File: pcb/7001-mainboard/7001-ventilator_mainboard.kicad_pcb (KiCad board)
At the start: 4 copper layers, 20 x 159.7 mm, 148 parts, among them J1 USB_B_Micro, J2 DNI (2211R-03G-SM-CR ), J3 Conn_01x02_MountingPin, J4 Conn_01x02_MountingPin, J5 Conn_01x02_MountingPin, Q1 IRLML6244TRPbF, Q10 SiA469DJ, Q2 IRLML6244TRPbF, Q3 IRLML6244TRPbF, Q4 2N7002P,215, Q5 2N7002P,215, Q6 DMP2035U, Q7 DMP2035U, Q8 2N7002P,215, Q9 2N7002P,215, SW1 SKQYABE010, U1 LPC11U37FBD48-401_, U10 MIC5501-3.0YM5, U11 NCP551SN50T1G, U12 74AHCT1G125SE, U2 MPXH6250AC6T1, U3 AT25SF041-SSHD-T, U5 TPS61087DSC, U6 BQ2002T, U7 TLV9001SIDBVR, U8 74AHCT1G125SE, U9 TPD2E2U06, Y1 MCSJK-7U-12.00-10-10-80-B-10

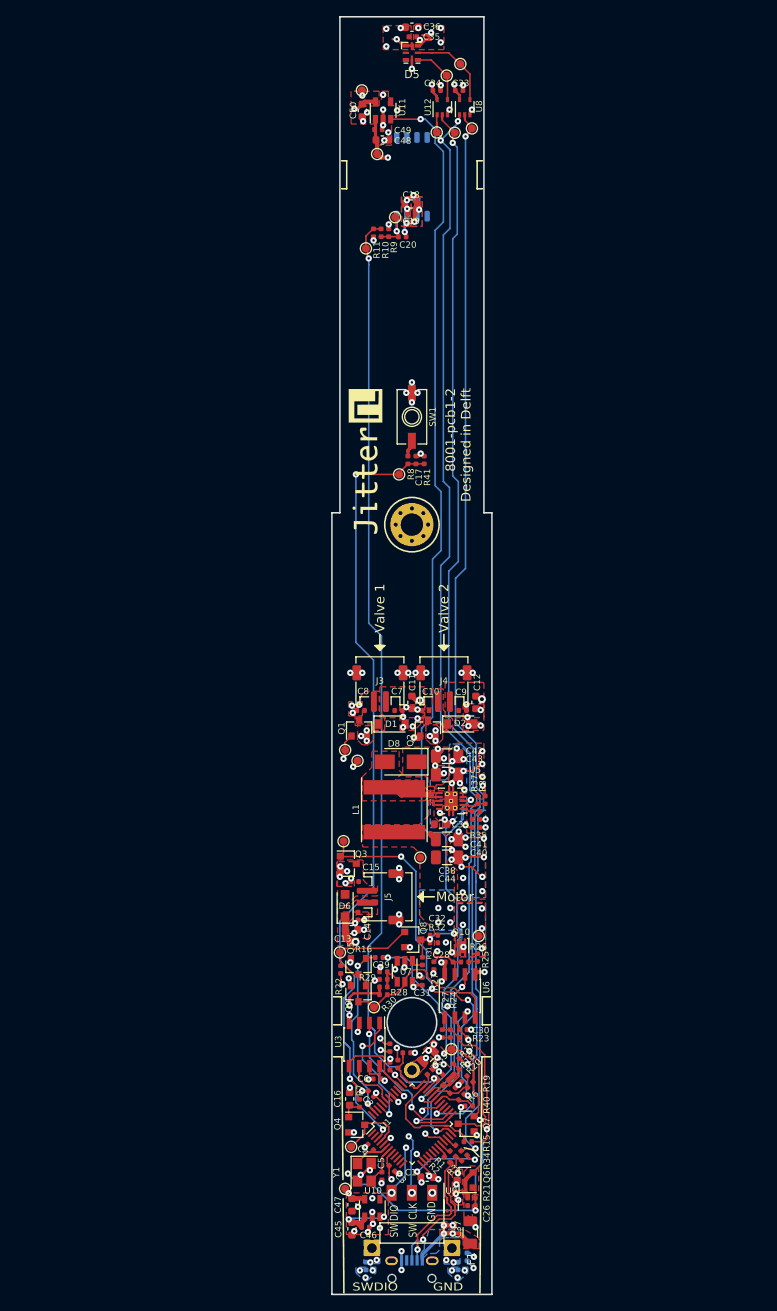
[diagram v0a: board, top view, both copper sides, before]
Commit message: Add 0-20mA for pressure regulator
The pressure regulator can be adjusted via 4-20mA (SPI via AD5410)
The regulator has an on-board pressure sensor giving 4-20mA feedback, which
we convert to 0.6-3.0V for the ADC.
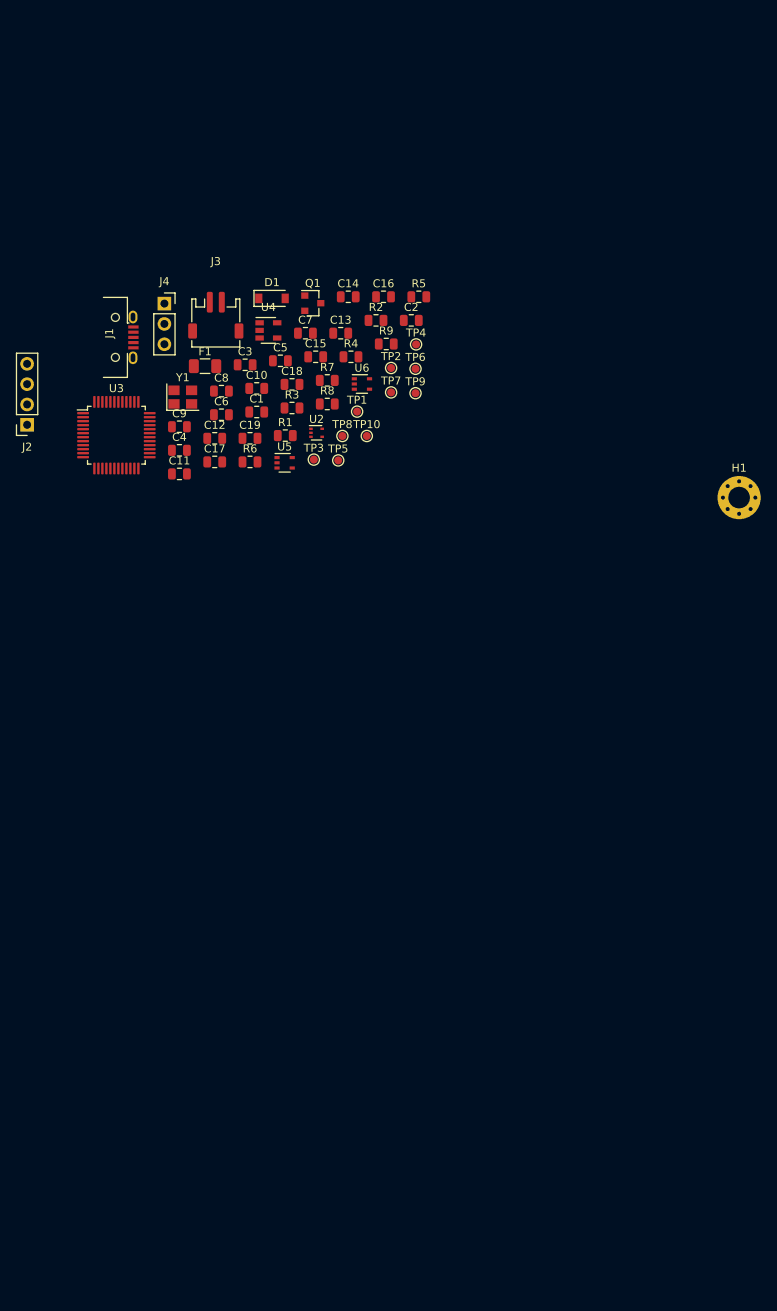
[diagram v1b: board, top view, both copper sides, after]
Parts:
- removed BT1: Battery, Jitter_Footprints:battery_varta_3V600HR
- removed C20: 47pF, Capacitor_SMD:C_0402_1005Metric
- removed C22, C24, C25, C27, C28, C29, C30, C31, C33, C34, C35, C37, C40, C46, C49: 100nF, Capacitor_SMD:C_0402_1005Metric
- removed C23, C26, C41, C51, C52: 2.2nF, Capacitor_SMD:C_0402_1005Metric
- removed C32: DNI, Capacitor_SMD:C_0402_1005Metric
- removed C36, C39, C45, C47, C48, C50: 1uF, Capacitor_SMD:C_0603_1608Metric
- removed C38, C42, C43, C44: 10uF eff, Capacitor_SMD:C_1206_3216Metric
- removed D2: BZT52C10+, Diode_SMD:D_SOD-123
- removed D5: APA102-2020, Jitter_Footprints:LED_APA102-2020
- removed D6: NRVTS245ESFT3G, Diode_SMD:D_SOD-123F
- removed D8: B340A-13-F, Diode_SMD:D_SMA
- removed G***: LOGO, Jitter_Logos:Jitter-med
- removed J5: Conn_01x02_MountingPin, Jitter_Footprints:JST_ZH_S2B-ZR-SM4A-TF_1x02-1MP_P1.5mm_Horizontal
- removed L1: 4.7uH, Jitter_Footprints:Inductor_Taiyo-Yuden_NR-8030
- removed Q10: SiA469DJ, Jitter_Footprints:Vishay_PowerPAK_SC70-6L_Single
- removed Q2, Q3: IRLML6244TRPbF, Package_TO_SOT_SMD:SOT-23
- removed Q4, Q5, Q8, Q9: 2N7002P,215, Package_TO_SOT_SMD:SOT-23
- removed Q6, Q7: DMP2035U, Package_TO_SOT_SMD:SOT-23
- removed R10, R36: 68k, Resistor_SMD:R_0402_1005Metric
- removed R11, R21, R32: 100k, Resistor_SMD:R_0402_1005Metric
- removed R15, R16, R18, R20, R25, R26, R27, R28, R30, R41: 1M, Resistor_SMD:R_0402_1005Metric
- removed R17, R19: 680k, Resistor_SMD:R_0402_1005Metric
- removed R22, R23, R24: 12k, Resistor_SMD:R_0402_1005Metric
- removed R29: 11k, Resistor_SMD:R_0402_1005Metric
- removed R31, R34: 100, Resistor_SMD:R_0402_1005Metric
- removed R33: 0.056, Resistor_SMD:R_0805_2012Metric
- removed R35: 8.2k, Resistor_SMD:R_0402_1005Metric
- removed R37: 17.4k, Resistor_SMD:R_0402_1005Metric
- removed R38, R39, R40: 4.7k, Resistor_SMD:R_0402_1005Metric
- removed SW1: SKQYABE010, Jitter_Footprints:SW_SPST_SKQYABE010
- removed TH1: B57230V2103F260 (10K), Resistor_SMD:R_0402_1005Metric
- removed TP11: valve_1_fet, TestPoint:TestPoint_Pad_D1.0mm
- removed TP12: valve_2_fet, TestPoint:TestPoint_Pad_D1.0mm
- removed TP13: motor_fet, TestPoint:TestPoint_Pad_D1.0mm
- removed TP14: sensor_out, TestPoint:TestPoint_Pad_D1.0mm
- removed TP15: pressure_level, TestPoint:TestPoint_Pad_D1.0mm
- removed TP16: LED_~CS~, TestPoint:TestPoint_Pad_D1.0mm
- removed TP17: LED_CLK, TestPoint:TestPoint_Pad_D1.0mm
- removed TP18: LED_MOSI, TestPoint:TestPoint_Pad_D1.0mm
- removed TP19: LED_clk_5V, TestPoint:TestPoint_Pad_D1.0mm
- removed TP20: LED_data_5V, TestPoint:TestPoint_Pad_D1.0mm
- removed U1: LPC11U37FBD48-401_, Package_QFP:LQFP-48_7x7mm_P0.5mm
- removed U10: MIC5501-3.0YM5, Package_TO_SOT_SMD:SOT-23-5
- removed U11: NCP551SN50T1G, Package_TO_SOT_SMD:SOT-23-5
- removed U12, U8: 74AHCT1G125SE, Package_TO_SOT_SMD:SOT-353_SC-70-5
- removed U7: TLV9001SIDBVR, Jitter_Footprints:TSOT-23-6
- removed U9: TPD2E2U06, Package_TO_SOT_SMD:SOT-553
- added U4: MIC5501-3.0YM5, Package_TO_SOT_SMD:SOT-23-5, F.Cu at (92.1, 59.2)
- C1, C11, C16: value 1uF -> 100nF; footprint Capacitor_SMD:C_0603_1608Metric -> Capacitor_SMD:C_0805_2012Metric
- C10: value 2.2nF -> 18pF; footprint Capacitor_SMD:C_0402_1005Metric -> Capacitor_SMD:C_0805_2012Metric
- C12: value 1uF -> 18pF; footprint Capacitor_SMD:C_0603_1608Metric -> Capacitor_SMD:C_0805_2012Metric
- C13, C18: footprint Capacitor_SMD:C_0603_1608Metric -> Capacitor_SMD:C_0805_2012Metric
- C14: value 2.2nF -> 100nF; footprint Capacitor_SMD:C_0402_1005Metric -> Capacitor_SMD:C_0805_2012Metric
- C15: value 2.2nF -> 1uF; footprint Capacitor_SMD:C_0402_1005Metric -> Capacitor_SMD:C_0805_2012Metric
- C17, C2, C3, C6, C7, C9: footprint Capacitor_SMD:C_0402_1005Metric -> Capacitor_SMD:C_0805_2012Metric
- C19: value 100nF -> 2.2nF; footprint Capacitor_SMD:C_0402_1005Metric -> Capacitor_SMD:C_0805_2012Metric
- C4, C5: value 18pF -> 1uF; footprint Capacitor_SMD:C_0402_1005Metric -> Capacitor_SMD:C_0805_2012Metric
- C8: value 2.2nF -> 47pF; footprint Capacitor_SMD:C_0402_1005Metric -> Capacitor_SMD:C_0805_2012Metric
- J1: moved to F.Cu
- J2: value DNI (2211R-03G-SM-CR ) -> SWD; footprint Jitter_Footprints:header_3x2.54_right_angle -> Connector_PinSocket_2.54mm:PinSocket_1x04_P2.54mm_Vertical
- J4: value Conn_01x02_MountingPin -> DNI; footprint Jitter_Footprints:JST_ZH_S2B-ZR-SM4A-TF_1x02-1MP_P1.5mm_Horizontal -> Connector_PinSocket_2.54mm:PinSocket_1x03_P2.54mm_Vertical
- R1: value 33R -> 68k; footprint Resistor_SMD:R_0402_1005Metric -> Resistor_SMD:R_0805_2012Metric
- R2: value 33R -> 100k; footprint Resistor_SMD:R_0402_1005Metric -> Resistor_SMD:R_0805_2012Metric
- R3, R6: footprint Resistor_SMD:R_0402_1005Metric -> Resistor_SMD:R_0805_2012Metric
- R4, R5: value 1k -> 33R; footprint Resistor_SMD:R_0402_1005Metric -> Resistor_SMD:R_0805_2012Metric
- R7: value 1M -> 4.7k; footprint Resistor_SMD:R_0402_1005Metric -> Resistor_SMD:R_0805_2012Metric
- R8: value 1k -> 1k5; footprint Resistor_SMD:R_0402_1005Metric -> Resistor_SMD:R_0805_2012Metric
- R9: value DNI (51k?) -> 1k5; footprint Resistor_SMD:R_0402_1005Metric -> Resistor_SMD:R_0805_2012Metric
- TP1: value ~ISP~ -> Reset
- TP10: value 5V -> valve_2_fet
- TP2: value Reset -> sensor_out
- TP3: value Vbus -> pressure_level
- TP4: value USB_~pwr_en~ -> LED_~CS~
- TP5: value unregulated_pwr -> 3V
- TP6: value charge_constant_current -> LED_CLK
- TP7: value V_battery -> LED_clk_5V
- TP8: value 3V -> LED_MOSI
- TP9: value 6V -> LED_data_5V
- U2: value MPXH6250AC6T1 -> TPD2E2U06; footprint Jitter_Footprints:MPXH6250AC -> Package_TO_SOT_SMD:SOT-553; moved to F.Cu
- U3: value AT25SF041-SSHD-T -> LPC11U37FBD48-401_; footprint Package_SO:SOIC-8_3.9x4.9mm_P1.27mm -> Package_QFP:LQFP-48_7x7mm_P0.5mm
- U5: value TPS61087DSC -> 74AHCT1G125SE; footprint Package_SON:VSON-10-1EP_3x3mm_P0.5mm_EP1.65x2.4mm_ThermalVias -> Package_TO_SOT_SMD:SOT-353_SC-70-5
- U6: value BQ2002T -> 74AHCT1G125SE; footprint Package_SO:SOIC-8_3.9x4.9mm_P1.27mm -> Package_TO_SOT_SMD:SOT-353_SC-70-5
- moved J1 125.8 mm to (70.9, 60.1), turned to 0 degrees
- moved F1 113.2 mm to (84.1, 63.7), turned to 0 degrees
- moved J2 107.4 mm to (61.9, 71.0)
- moved R2 105.3 mm to (105.5, 58.0), turned to 0 degrees
- moved C5 102.7 mm to (93.6, 63.0), turned to 0 degrees
- moved C3 102.1 mm to (89.2, 63.5), turned to 0 degrees
- moved C16 100.4 mm to (106.5, 55.0), turned to 0 degrees
- moved Y1 99.5 mm to (81.4, 67.5), turned to 0 degrees
- moved C1 98.0 mm to (90.6, 69.4)
- moved C2 96.8 mm to (109.9, 58.0), turned to 0 degrees
- moved R3 96.2 mm to (95.0, 68.9), turned to 0 degrees
- moved R5 95.9 mm to (110.9, 55.0), turned to 0 degrees
- moved TP8 94.1 mm to (101.3, 72.4)
- moved R1 92.2 mm to (94.2, 72.3), turned to 0 degrees
- moved TP1 91.9 mm to (103.2, 69.3)
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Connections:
- C1 pad 1: +3V -> Net-(C1-Pad1)
- C10 pad 1: Net-(C10-Pad1) -> /XTAL_IN
- C11 pad 1: +6V -> +5V
- C12 pad 1: +6V -> /XTAL_OUT
- C13 pad 1: +6V -> +5V
- C14 pad 1: +6V -> +5V
- C15 pad 1: Net-(C15-Pad1) -> +3V3
- C16 pad 1: GND -> +5V
- C16 pad 2: Net-(C16-Pad2) -> GND
- C17 pad 1: /MCU/button -> +6V
- C18 pad 1: +5V -> +6V
- C19 pad 1: +5V -> Net-(C19-Pad1)
- C2 pad 1: +3V -> +3V3
- C3 pad 1: +3V -> +3V3
- C4 pad 1: /MCU/XTAL_IN -> +3V3
- C5 pad 1: /MCU/XTAL_OUT -> +5V
- C6 pad 1: +3V -> +5V
- C7 pad 1: +6V -> /~RESET~
- C8 pad 1: Net-(C8-Pad1) -> /pressure_sensor_out
- C9 pad 1: +6V -> /pressure_level
- D1 pad 1: Net-(C8-Pad1) -> Net-(C19-Pad1)
- F1 pad 1: Net-(C37-Pad1) -> Net-(C1-Pad1)
- F1 pad 2: /Battery & Power Select/Vbus -> +5V
- J1 pad 1: Net-(C37-Pad1) -> Net-(C1-Pad1)
- J1 pad 2: /MCU/USB_DN -> /USB_DN
- J1 pad 3: /MCU/USB_DP -> /USB_DP
- J1 pad 4: Net-(J1-Pad4) -> (no net)
- J2 pad 2: /MCU/SWCLK -> /SWCLK
- J2 pad 3: /MCU/SWDIO -> /SWDIO
- J3 pad 2: Net-(C8-Pad1) -> Net-(C19-Pad1)
- J4 pad 1: +6V -> GND
- J4 pad 2: Net-(C10-Pad1) -> /~ISP~
- Q1 pad 3: Net-(C8-Pad1) -> Net-(C19-Pad1)
- R1 pad 1: /MCU/USB_DP -> /pressure_level
- R1 pad 2: Net-(R1-Pad2) -> /pressure_sensor_out
- R2 pad 1: /MCU/USB_DN -> GND
- R2 pad 2: Net-(R2-Pad2) -> /pressure_level
- R3 pad 1: /MCU/USB_DP -> /USB_DP
- R3 pad 2: +3V -> +3V3
- R4 pad 1: Net-(Q1-Pad1) -> /USB_DP
- R4 pad 2: /MCU/valve_1 -> Net-(R4-Pad2)
- R5 pad 1: Net-(Q2-Pad1) -> /USB_DN
- R5 pad 2: /MCU/valve_2 -> Net-(R5-Pad2)
- R6 pad 1: Net-(Q3-Pad1) -> Net-(Q1-Pad1)
- R6 pad 2: /MCU/motor -> /pwm_1
- R7 pad 1: Net-(C16-Pad2) -> GND
- R7 pad 2: /MCU/button -> /pwm_1
- R8 pad 1: /MCU/button -> /I2C_SCL
- R8 pad 2: Net-(R8-Pad2) -> +5V
- R9 pad 1: GND -> /I2C_SDA
- R9 pad 2: /sensor/pressure_sensor_out -> +5V
- TP1 pad 1: /MCU/button_~ISP~ -> /~RESET~
- TP10 pad 1: +5V -> Net-(Q1-Pad1)
- TP2 pad 1: /MCU/button -> /pressure_sensor_out
- TP3 pad 1: /Battery & Power Select/Vbus -> /pressure_level
- TP4 pad 1: /Battery & Power Select/USB_~pwr_en~ -> /LED_~CS~
- TP5 pad 1: /Battery & Power Select/unregulated_pwr -> +3V3
- TP6 pad 1: /Battery & Power Select/charge_constant_current -> /LED_CLK
- TP7 pad 1: /Battery & Power Select/V_battery -> /LED_clock_5V
- TP8 pad 1: +3V -> /LED_MOSI
- TP9 pad 1: +6V -> /LED_data_5V
- U2 pad 1: Net-(U2-Pad1) -> (no net)
- U2 pad 2: +5V -> /USB_DN
- U2 pad 3: GND -> /USB_DP
- U2 pad 4: /sensor/pressure_sensor_out -> GND
- U2 pad 5: Net-(U2-Pad5) -> /USB_DN
- U3 pad 1: /MCU/flash_~CS~ -> (no net)
- U3 pad 2: /MCU/flash_MISO -> (no net)
- U3 pad 3: +3V -> /~RESET~
- U3 pad 4: GND -> /~ISP~
- U3 pad 5: /MCU/flash_MOSI -> GND
- U3 pad 6: /MCU/flash_CLK -> /XTAL_IN
- U3 pad 7: +3V -> /XTAL_OUT
- U3 pad 8: +3V -> +3V3
- U5 pad 1: /Power regulation/DCDC_COMP -> /LED_~CS~
- U5 pad 2: /Power regulation/DCDC_FB -> /LED_CLK
- U5 pad 3: /MCU/DCDC_en -> GND
- U5 pad 4: GND -> /LED_clock_5V
- U5 pad 5: GND -> +5V
- U6 pad 1: GND -> /LED_~CS~
- U6 pad 2: /Battery & Power Select/charger_status -> /LED_MOSI
- U6 pad 3: Net-(C28-Pad1) -> GND
- U6 pad 4: GND -> /LED_data_5V
- U6 pad 5: /Battery & Power Select/chg_temp -> +5V
- Y1 pad 1: /MCU/XTAL_IN -> /XTAL_IN
- Y1 pad 3: /MCU/XTAL_OUT -> /XTAL_OUT
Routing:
- net /MCU/DCDC_en: track 144.3 -> 0.00 mm, vias 3 -> 0
- net /MCU/LED_~CS~: track 142.9 -> 0.00 mm, vias 4 -> 0
- net /MCU/LED_CLK: track 136.2 -> 0.00 mm, vias 2 -> 0
- net /MCU/LED_MOSI: track 135.1 -> 0.00 mm, vias 2 -> 0
- net GND: track 120.7 -> 0.00 mm, vias 158 -> 0
- net /MCU/pressure_level: track 119.0 -> 0.00 mm, vias 2 -> 0
- net +6V: track 112.6 -> 0.00 mm, vias 9 -> 0
- net +3V: track 103.1 -> 0.00 mm, vias 10 -> 0
- net /MCU/button: track 102.5 -> 0.00 mm, vias 3 -> 0
- net /Battery & Power Select/unregulated_pwr: track 62.0 -> 0.00 mm, vias 12 -> 0
- net Net-(C26-Pad2): track 58.3 -> 0.00 mm, vias 4 -> 0
- net +5V: track 54.0 -> 0.00 mm, vias 11 -> 0
- net /Battery & Power Select/Vbus: track 52.8 -> 0.00 mm, vias 4 -> 0
- net Net-(Q2-Pad1): track 52.6 -> 0.00 mm, vias 3 -> 0
- net Net-(Q3-Pad1): track 46.5 -> 0.00 mm, vias 4 -> 0
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- removed copper zone on B.Cu, net +5V
- removed copper zone on F.Cu, net +5V
- removed copper zone on mid, net +5V
- removed copper zone on F.Cu, net +6V
- removed copper zone on mid, net +6V
- removed copper zone on B.Cu, net /Battery & Power Select/V_battery
- removed copper zone on F.Cu, net /Battery & Power Select/V_battery
- removed copper zone on mid, net /Battery & Power Select/V_battery
- removed copper zone on F.Cu, net /Battery & Power Select/Vbus
- removed copper zone on B.Cu, net /Battery & Power Select/unregulated_pwr
- removed copper zone on F.Cu, net /Battery & Power Select/unregulated_pwr
- removed copper zone on mid, net /Battery & Power Select/unregulated_pwr
- removed copper zone on F.Cu, net /Power regulation/DCDC_SW
- removed copper zone on B.Cu, net GND
- removed copper zone on F.Cu, net GND
- removed copper zone on GND, net GND
- removed copper zone on F.Cu, net Net-(BT1-Pad2)
- removed copper zone on F.Cu, net Net-(C10-Pad1)
- removed copper zone on F.Cu, net Net-(C15-Pad1)
- removed copper zone on B.Cu, net Net-(C37-Pad1)
- removed copper zone on F.Cu, net Net-(C37-Pad1)
- removed copper zone on F.Cu, net Net-(C8-Pad1)
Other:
- board outline removed
- board text removed: "5V"
- board text removed: "8001-pcb1-2 Designed in Delft"
- board text removed: "<- Snap-fit clearance"
- board text removed: "CLK"
- board text removed: "DIO"
- board text removed: "GND"
- board text removed: "Keepout"
- board text removed: "Keepout: debug"
- board text removed: "Motor"
- board text removed: "Preferably no components in this area, < 1mm height (except button)"
- board text removed: "SW"
- board text removed: "SWDIO"
- board text removed: "Snap-fit clearance ->"
- board text removed: "Valve 1"
- board text removed: "Valve 2"
- board text removed: "max component height +/-1.2mm?"
- board text removed: "max component height 4-5mm (check 3D assembly)"

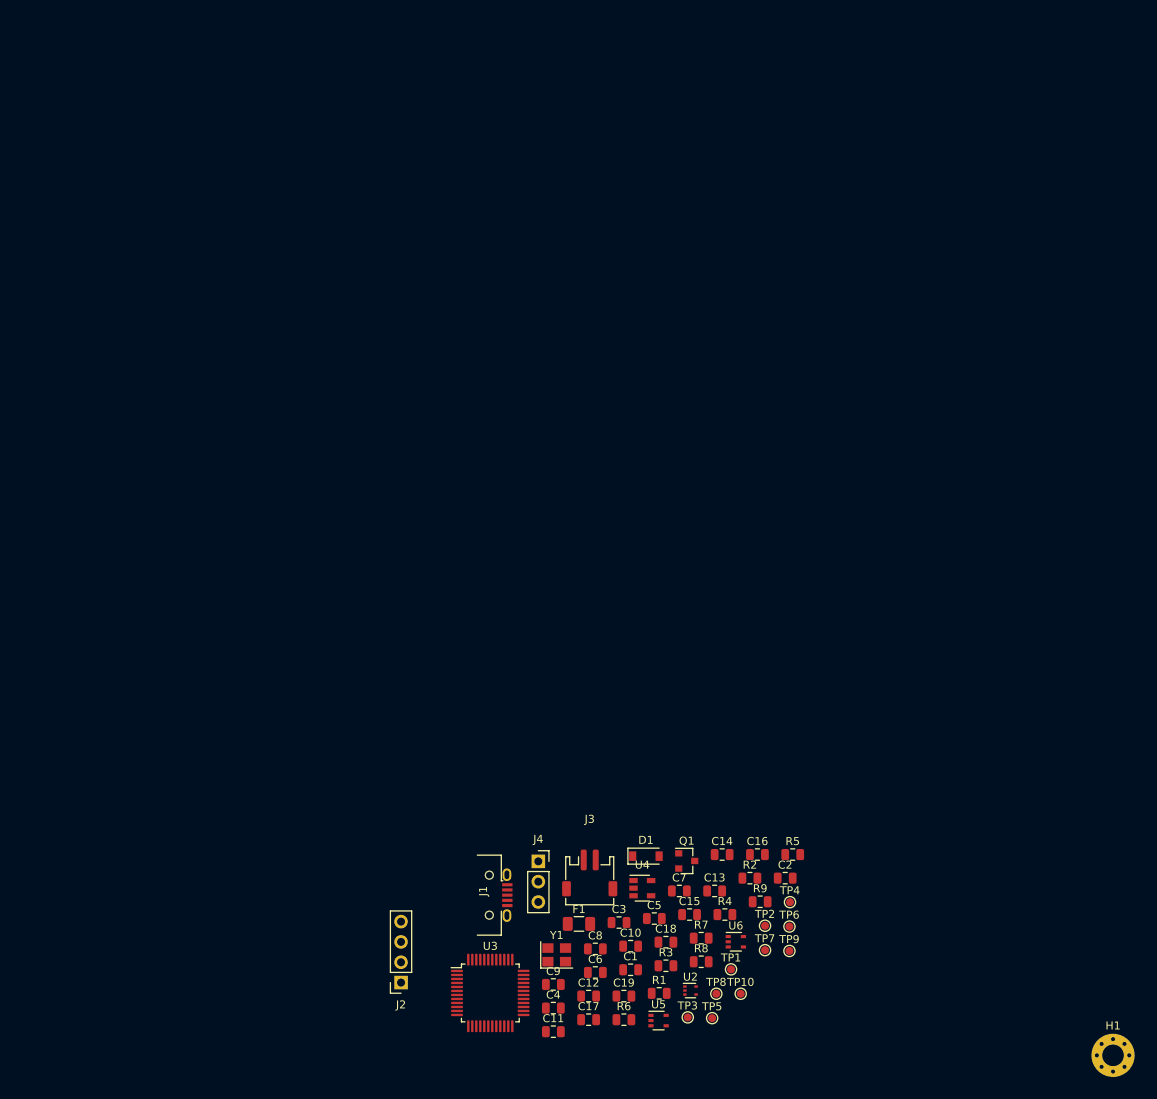
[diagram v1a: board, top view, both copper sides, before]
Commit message: Schematics: add pressure sensors
The design allows 2 pressure sensors: 'sensor 1' and 'sensor 2'.

Only sensor 1 is required. Sensor 2 can be left out, but may be placed in case of
changing requirements in the future (e.g. using 2 sensors to measure
flow).

Each of the sensors may be implemented by choosing one of 3 different footprints.
On the PCB layout, these 3 footprints will be overlapped to create a
'universal' pressure sensor footprint.
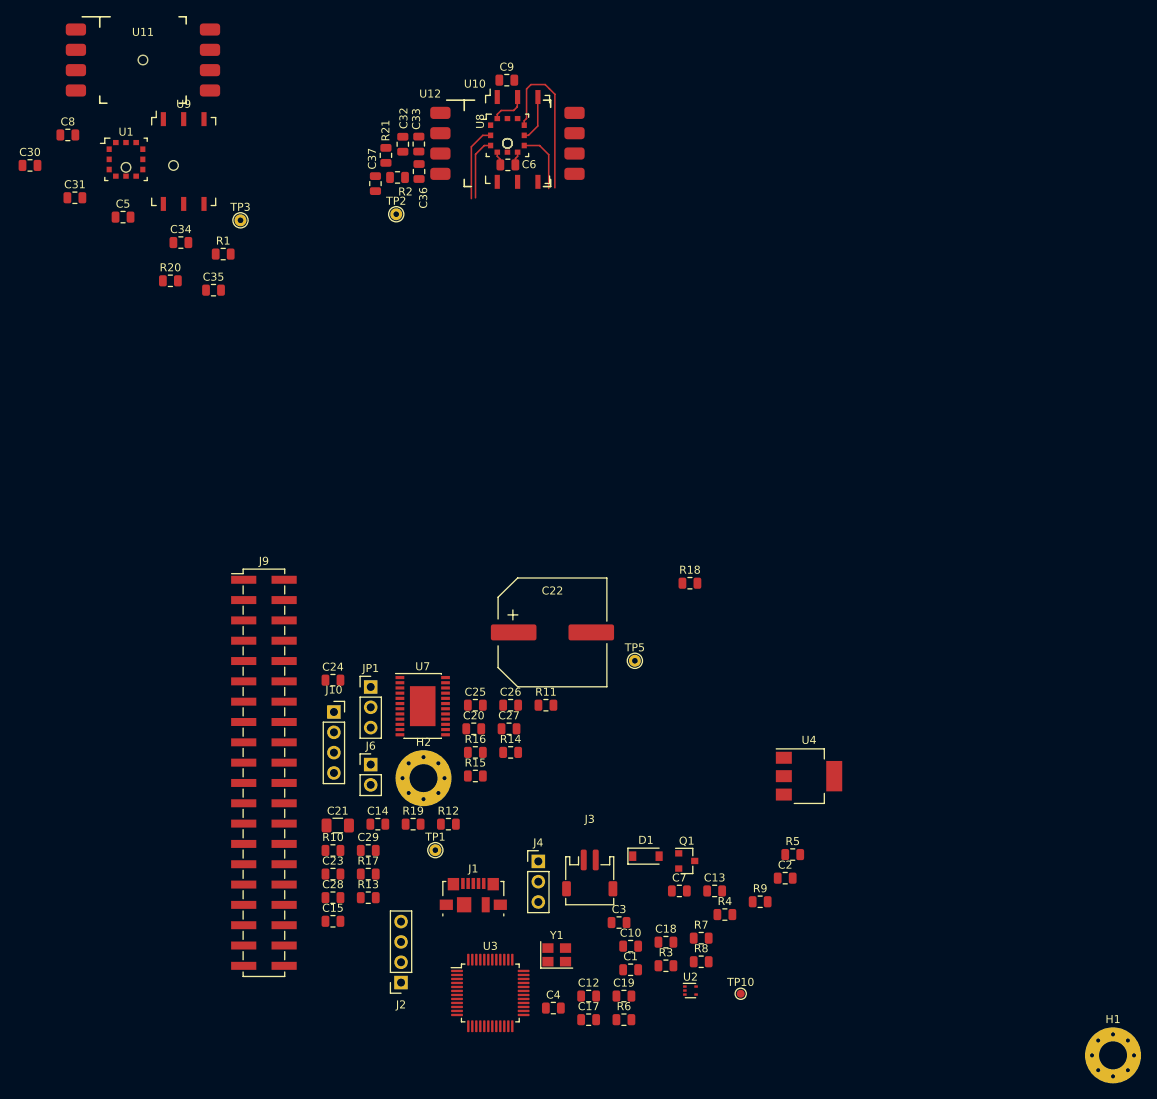
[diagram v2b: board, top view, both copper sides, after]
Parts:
- removed C11, C16: 100nF, Capacitor_SMD:C_0805_2012Metric
- removed F1: MCCFB1206TFF/2, Resistor_SMD:R_1206_3216Metric
- removed TP4: LED_~CS~, TestPoint:TestPoint_Pad_D1.0mm
- removed TP6: LED_CLK, TestPoint:TestPoint_Pad_D1.0mm
- removed TP7: LED_clk_5V, TestPoint:TestPoint_Pad_D1.0mm
- removed TP8: LED_MOSI, TestPoint:TestPoint_Pad_D1.0mm
- removed TP9: LED_data_5V, TestPoint:TestPoint_Pad_D1.0mm
- removed U5, U6: 74AHCT1G125SE, Package_TO_SOT_SMD:SOT-353_SC-70-5
- added C20: 100nF 50V, Capacitor_SMD:C_0805_2012Metric, F.Cu at (71.0, 39.3)
- added C21: 10uF 50V, Capacitor_SMD:C_1206_3216Metric, F.Cu at (54.0, 51.4)
- added C22: 330uF, Jitter_Footprints:CP_Elec_12.5x13.5, F.Cu at (80.8, 27.2)
- added C23: 10nF, Capacitor_SMD:C_0805_2012Metric, F.Cu at (53.4, 57.4)
- added C24: 100nF 50V, Capacitor_SMD:C_0805_2012Metric, F.Cu at (53.4, 33.2)
- added C25: 10uF, Capacitor_SMD:C_0805_2012Metric, F.Cu at (71.2, 36.3)
- added C26: 100nF, Capacitor_SMD:C_0805_2012Metric, F.Cu at (75.6, 36.3)
- added C27: 10nF, Capacitor_SMD:C_0805_2012Metric, F.Cu at (75.4, 39.3)
- added C28: 100nF, Capacitor_SMD:C_0805_2012Metric, F.Cu at (53.4, 60.4)
- added C29: 100nF, Capacitor_SMD:C_0805_2012Metric, F.Cu at (57.8, 54.5)
- added C30: 1uF, Capacitor_SMD:C_0805_2012Metric, F.Cu at (15.5, -31.1)
- added C31: 100nF, Capacitor_SMD:C_0805_2012Metric, F.Cu at (21.1, -27.1)
- added C32: 1uF, Capacitor_SMD:C_0805_2012Metric, F.Cu at (62.1, -33.8)
- added C33: 100nF, Capacitor_SMD:C_0805_2012Metric, F.Cu at (64.1, -33.8)
- added C34: 470pF, Capacitor_SMD:C_0805_2012Metric, F.Cu at (34.4, -21.5)
- added C35: 2.2nF, Capacitor_SMD:C_0805_2012Metric, F.Cu at (38.5, -15.6)
- added C36: 470pF, Capacitor_SMD:C_0805_2012Metric, F.Cu at (64.2, -30.4)
- added C37: 2.2nF, Capacitor_SMD:C_0805_2012Metric, F.Cu at (58.7, -28.9)
- added H2: DNI (mounting hole), MountingHole:MountingHole_3.5mm_Pad_Via, F.Cu at (64.7, 45.5)
- added J10: UART, Connector_PinSocket_2.54mm:PinSocket_1x04_P2.54mm_Vertical, F.Cu at (53.5, 37.2)
- added J6: 5V out, Connector_PinHeader_2.54mm:PinHeader_1x02_P2.54mm_Vertical, F.Cu at (58.1, 43.8)
- added J9: Raspberry_Pi_2_3, Connector_PinHeader_2.54mm:PinHeader_2x20_P2.54mm_Vertical_SMD, F.Cu at (44.8, 44.8)
- added JP1: 5V_jumper, Connector_PinHeader_2.54mm:PinHeader_1x03_P2.54mm_Vertical, F.Cu at (58.1, 34.0)
- added R10: 10k, Resistor_SMD:R_0805_2012Metric, F.Cu at (53.4, 54.5)
- added R11: 0, Resistor_SMD:R_0805_2012Metric, F.Cu at (80.0, 36.3)
- added R12: 10k, Resistor_SMD:R_0805_2012Metric, F.Cu at (67.8, 51.2)
- added R13: 0, Resistor_SMD:R_0805_2012Metric, F.Cu at (57.8, 60.4)
- added R14: DNI, Resistor_SMD:R_0805_2012Metric, F.Cu at (75.6, 42.2)
- added R15: 150, Resistor_SMD:R_0805_2012Metric, F.Cu at (71.2, 45.2)
- added R16: 0, Resistor_SMD:R_0805_2012Metric, F.Cu at (71.2, 42.2)
- added R17: 0, Resistor_SMD:R_0805_2012Metric, F.Cu at (57.8, 57.4)
- added R18: 0, Resistor_SMD:R_0805_2012Metric, F.Cu at (98.0, 21.1)
- added R19: DNI, Resistor_SMD:R_0805_2012Metric, F.Cu at (63.4, 51.2)
- added R20: 100k, Resistor_SMD:R_0805_2012Metric, F.Cu at (33.1, -16.7)
- added R21: 100k, Resistor_SMD:R_0805_2012Metric, F.Cu at (60.0, -32.4)
- added U1: MPRLS0001PG0000SA, Jitter_Footprints:MPRLS0001PG0000SA, F.Cu at (27.5, -31.9)
- added U10: ABPMAND001PG2A3, Jitter_Footprints:ABPMXXX000XX0XX, F.Cu at (76.5, -34.4)
- added U11: MPVZ5010GW6U, Jitter_Footprints:MPVZ5010GW6U, F.Cu at (29.6, -44.3)
- added U12: MPVZ5010GW6U, Jitter_Footprints:MPVZ5010GW6U, F.Cu at (75.2, -33.9)
- added U7: AD5410AREZ, Jitter_Footprints:TSSOP-24-1EP_4.4x7.8mm_P0.65mm, F.Cu at (64.6, 36.5)
- added U8: MPRLS0001PG0000SA, Jitter_Footprints:MPRLS0001PG0000SA, F.Cu at (75.2, -34.9)
- added U9: ABPMAND001PG2A3, Jitter_Footprints:ABPMXXX000XX0XX, F.Cu at (34.7, -31.6)
- C13: value 1uF -> 4.7uF
- C14: value 100nF -> 10uF
- C15: value 1uF -> 100nF
- C5: value 1uF -> 1nF
- C6: value 100nF -> 1nF
- C8: value 47pF -> 100nF
- C9: value 2.2nF -> 100nF
- H1: footprint MountingHole:MountingHole_2.7mm_Pad_Via -> MountingHole:MountingHole_3.5mm_Pad_Via
- J1: footprint Jitter_Footprints:USB_Micro-B_UJ2-MIBH-4-SMT-TR-67_SMD_Horizontal -> Connector_USB:USB_Micro-B_Molex_47346-0001
- J4: footprint Connector_PinSocket_2.54mm:PinSocket_1x03_P2.54mm_Vertical -> Connector_PinHeader_2.54mm:PinHeader_1x03_P2.54mm_Vertical
- R2: value 100k -> 68k
- TP1: value Reset -> 5V; footprint TestPoint:TestPoint_Pad_D1.0mm -> TestPoint:TestPoint_THTPad_D1.5mm_Drill0.7mm
- TP2: value sensor_out -> TestPoint; footprint TestPoint:TestPoint_Pad_D1.0mm -> TestPoint:TestPoint_THTPad_D1.5mm_Drill0.7mm
- TP3: value pressure_level -> TestPoint; footprint TestPoint:TestPoint_Pad_D1.0mm -> TestPoint:TestPoint_THTPad_D1.5mm_Drill0.7mm
- TP5: value 3V -> 5V; footprint TestPoint:TestPoint_Pad_D1.0mm -> TestPoint:TestPoint_THTPad_D1.5mm_Drill0.7mm
- U4: value MIC5501-3.0YM5 -> MCP1825S; footprint Package_TO_SOT_SMD:SOT-23-5 -> Package_TO_SOT_SMD:SOT-223-3_TabPin2
- moved C8 121.2 mm to (20.2, -35.0)
- moved TP3 114.2 mm to (41.8, -24.3)
- moved C9 113.2 mm to (75.1, -41.8)
- moved C5 110.0 mm to (27.1, -24.7)
- moved R1 107.3 mm to (39.7, -20.1)
- moved C6 101.5 mm to (75.2, -31.2)
- moved TP2 100.2 mm to (61.3, -25.0)
- moved R2 98.0 mm to (61.5, -29.6)
- moved TP5 45.7 mm to (91.1, 30.8)
- moved C15 44.6 mm to (53.4, 63.3)
- moved C14 43.2 mm to (59.0, 51.2)
- moved TP1 39.9 mm to (66.2, 54.5)
- moved U4 25.1 mm to (112.9, 45.2)
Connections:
- net Net-(C1-Pad1) renamed /USB_VBUS
- net Net-(R4-Pad2) renamed /MCU_DP
- net Net-(R5-Pad2) renamed /MCU_DM
- C14 pad 1: +5V -> +3V3
- C5 pad 1: +5V -> Net-(C5-Pad1)
- C5 pad 2: GND -> Net-(C5-Pad2)
- C6 pad 1: +5V -> Net-(C6-Pad1)
- C6 pad 2: GND -> Net-(C6-Pad2)
- C8 pad 1: /pressure_sensor_out -> GND
- C8 pad 2: GND -> +3V3
- C9 pad 1: /pressure_level -> GND
- C9 pad 2: GND -> +3V3
- J2 pad 4: (no net) -> +3V
- R1 pad 1: /pressure_level -> /A_PRESSURE_1
- R1 pad 2: /pressure_sensor_out -> /pressure_sensor/MPVZ5010_1_OUT
- R2 pad 1: GND -> /A_PRESSURE_1
- R2 pad 2: /pressure_level -> /pressure_sensor/MPVZ5010_2_OUT
- R8 pad 2: +5V -> /V_PU
- R9 pad 2: +5V -> /V_PU
- TP1 pad 1: /~RESET~ -> +5V
- TP2 pad 1: /pressure_sensor_out -> /A_PRESSURE_1
- TP3 pad 1: /pressure_level -> /A_PRESSURE_1
- U3 pad 11: (no net) -> /UART_RX
- U3 pad 12: (no net) -> /UART_TX
- U4 pad 3: +5V -> +3V3
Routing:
- net /pressure_sensor/PSENSE_RESET: track 0.00 -> 20.6 mm
- net /PSENSE_SPI_MOSI: track 0.00 -> 9.48 mm
- net /PSENSE_SPI_CLK: track 0.00 -> 7.79 mm
- net /PSENSE_SPI_MISO: track 0.00 -> 7.77 mm
- net /PSENSE_2_DATA_READY: track 0.00 -> 5.89 mm
- net +3V3: track 0.00 -> 4.79 mm
- net Net-(C6-Pad2): track 0.00 -> 1.74 mm
- net Net-(C6-Pad1): track 0.00 -> 1.74 mm
